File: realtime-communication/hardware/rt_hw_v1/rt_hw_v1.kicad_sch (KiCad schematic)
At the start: 64 parts, among them J1 USB2UART, J6 ConnBattery, Q1 SS8050, Q2 SS8050, SW1 RST, SW3 Boot, SW4 5V_EN, SW9 PS Joystick, U1 74HCT245_TSSOP, U2 CH340C, U3 ESP32-S3-WROOM-1, U4 BQ27441-G1, U5 BQ24075RGT_DPPM, U6 TPS63002_SEPIC_5V, U7 ADS1115IDGS, U9 TPS63001_SEPIC_3V3

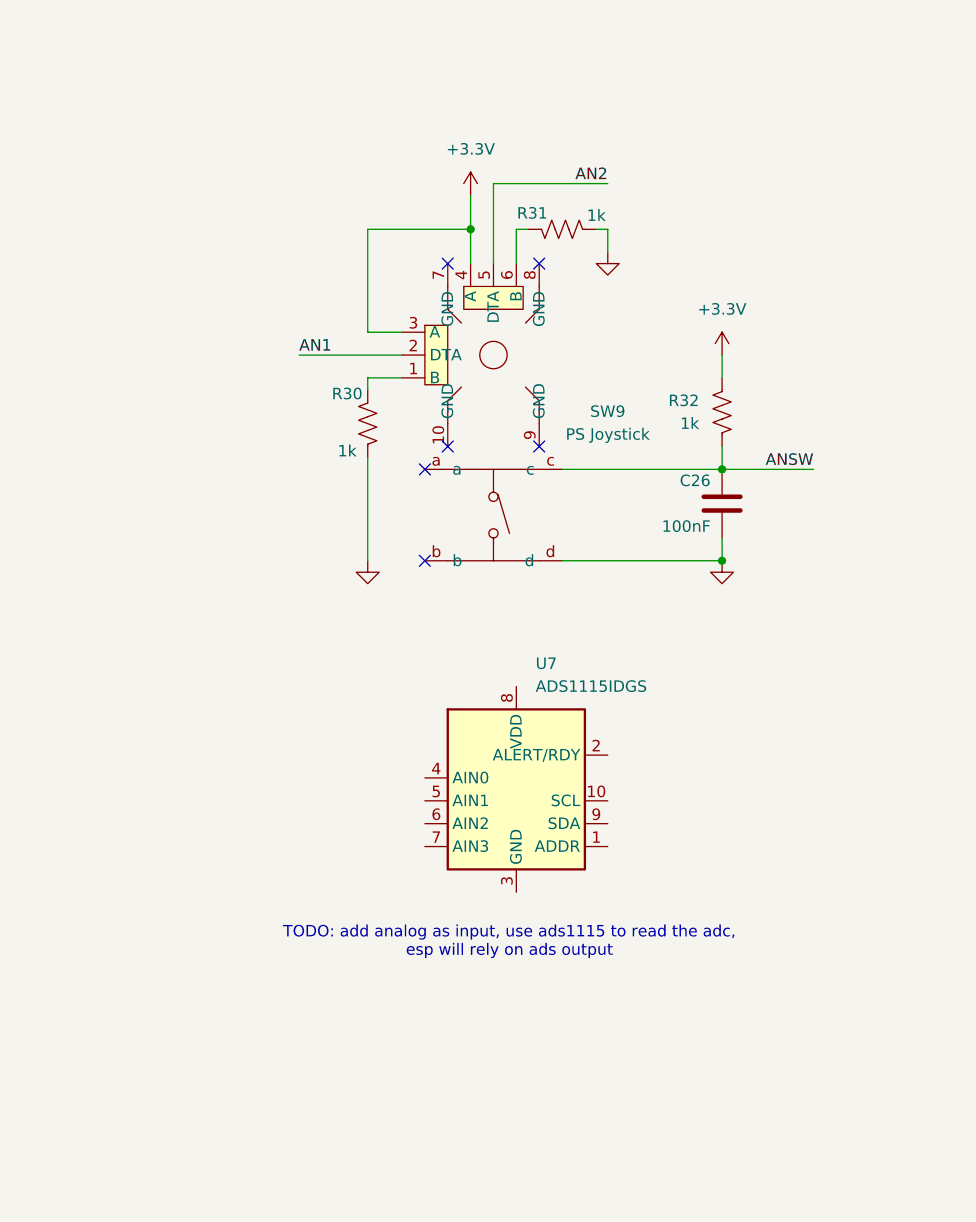
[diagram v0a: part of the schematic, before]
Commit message: add ads1115 from design block
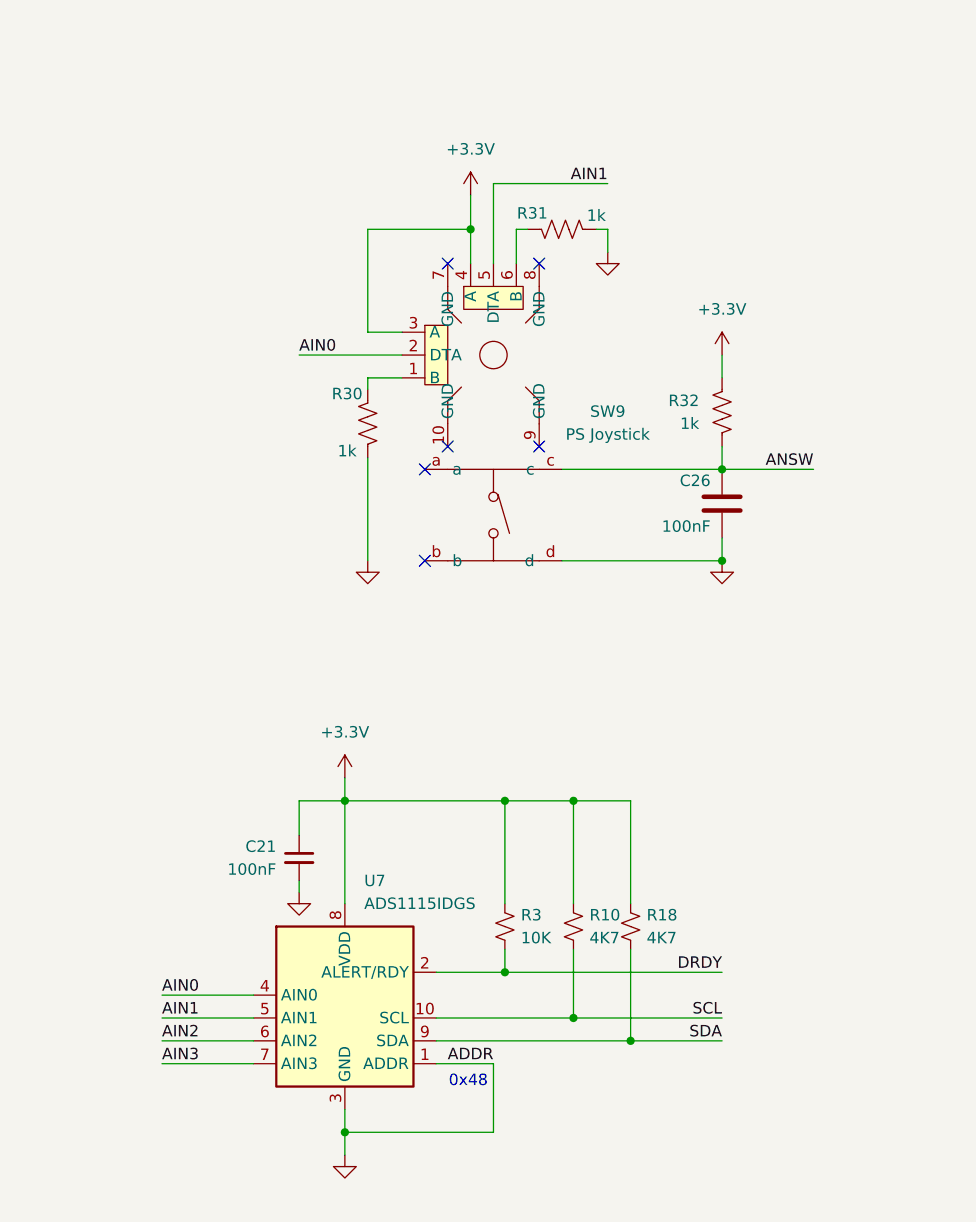
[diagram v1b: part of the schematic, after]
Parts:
- added C21: 100nF, Capacitor_SMD:C_0805_2012Metric, symbol Device:C_Small
- added R10, R18: 4K7, Resistor_SMD:R_0805_2012Metric, symbol Device:R_Small_US
- added R3: 10K, Resistor_SMD:R_0805_2012Metric, symbol Device:R_Small_US
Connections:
- net AN1 is gone; now on net AIN0: SW9.2 (DTA)
- net AN2 is gone; now on net AIN1: SW9.5 (DTA)
- net +3.3V: now also U7.8 (VDD), C21.1, R10.1, R18.1, R3.1
- net GND: now also U7.1 (ADDR), U7.3 (GND), C21.2
- net SCL: now reaches U7.10 (SCL)
- net SCL: now also R10.2
- net DRDY: now reaches U7.2 (ALERT/RDY)
- net DRDY: now also R3.2
- net AIN0: now reaches U7.4 (AIN0)
- net AIN1: now reaches U7.5 (AIN1)
- net AIN2: now reaches U7.6 (AIN2)
- net AIN3: now reaches U7.7 (AIN3)
- net SDA: now reaches U7.9 (SDA)
- net SDA: now also R18.2
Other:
- note added: "0x48"
- note removed: "TODO: add analog as input, use ads1115 to read the adc, esp will rely on ads output"

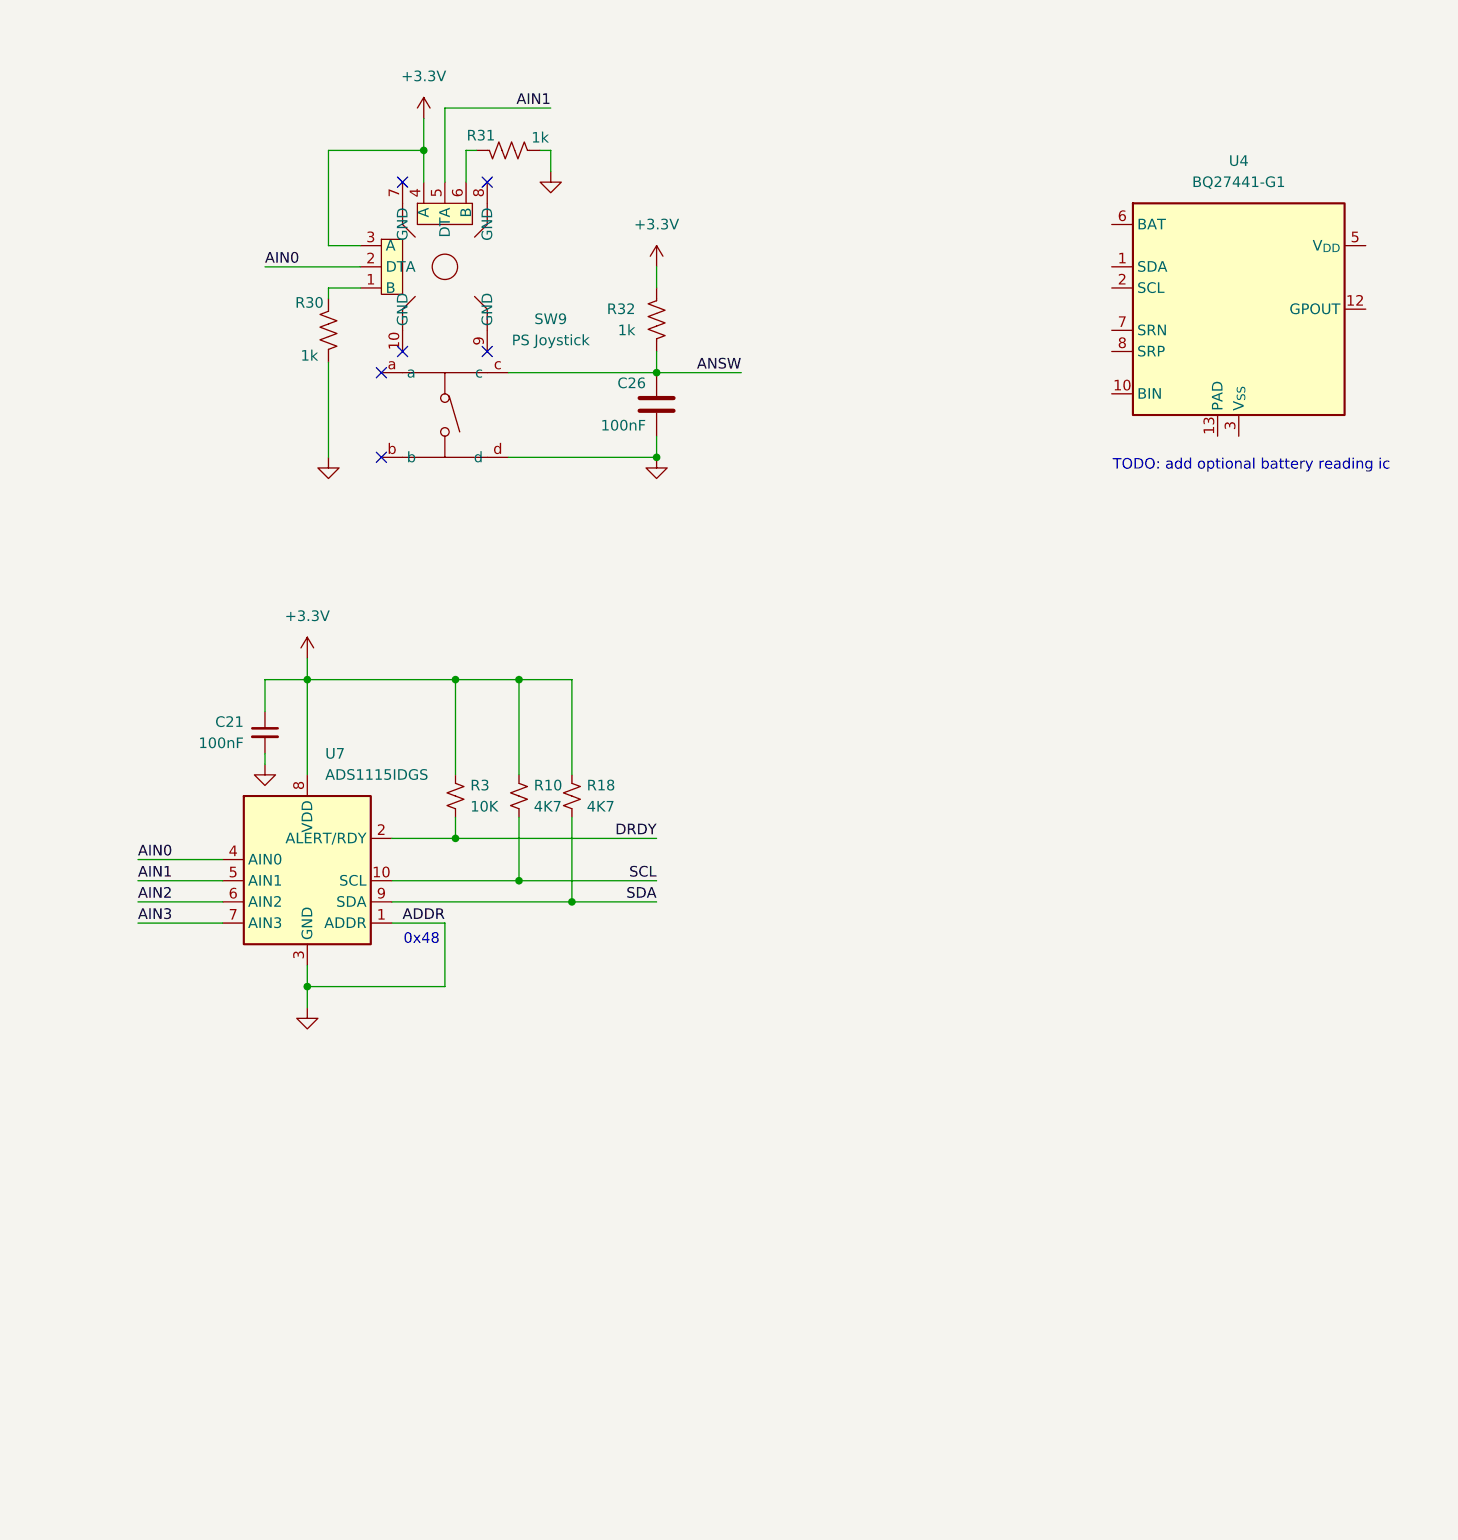
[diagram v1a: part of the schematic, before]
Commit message: add bq27441 single batt fuel gauge
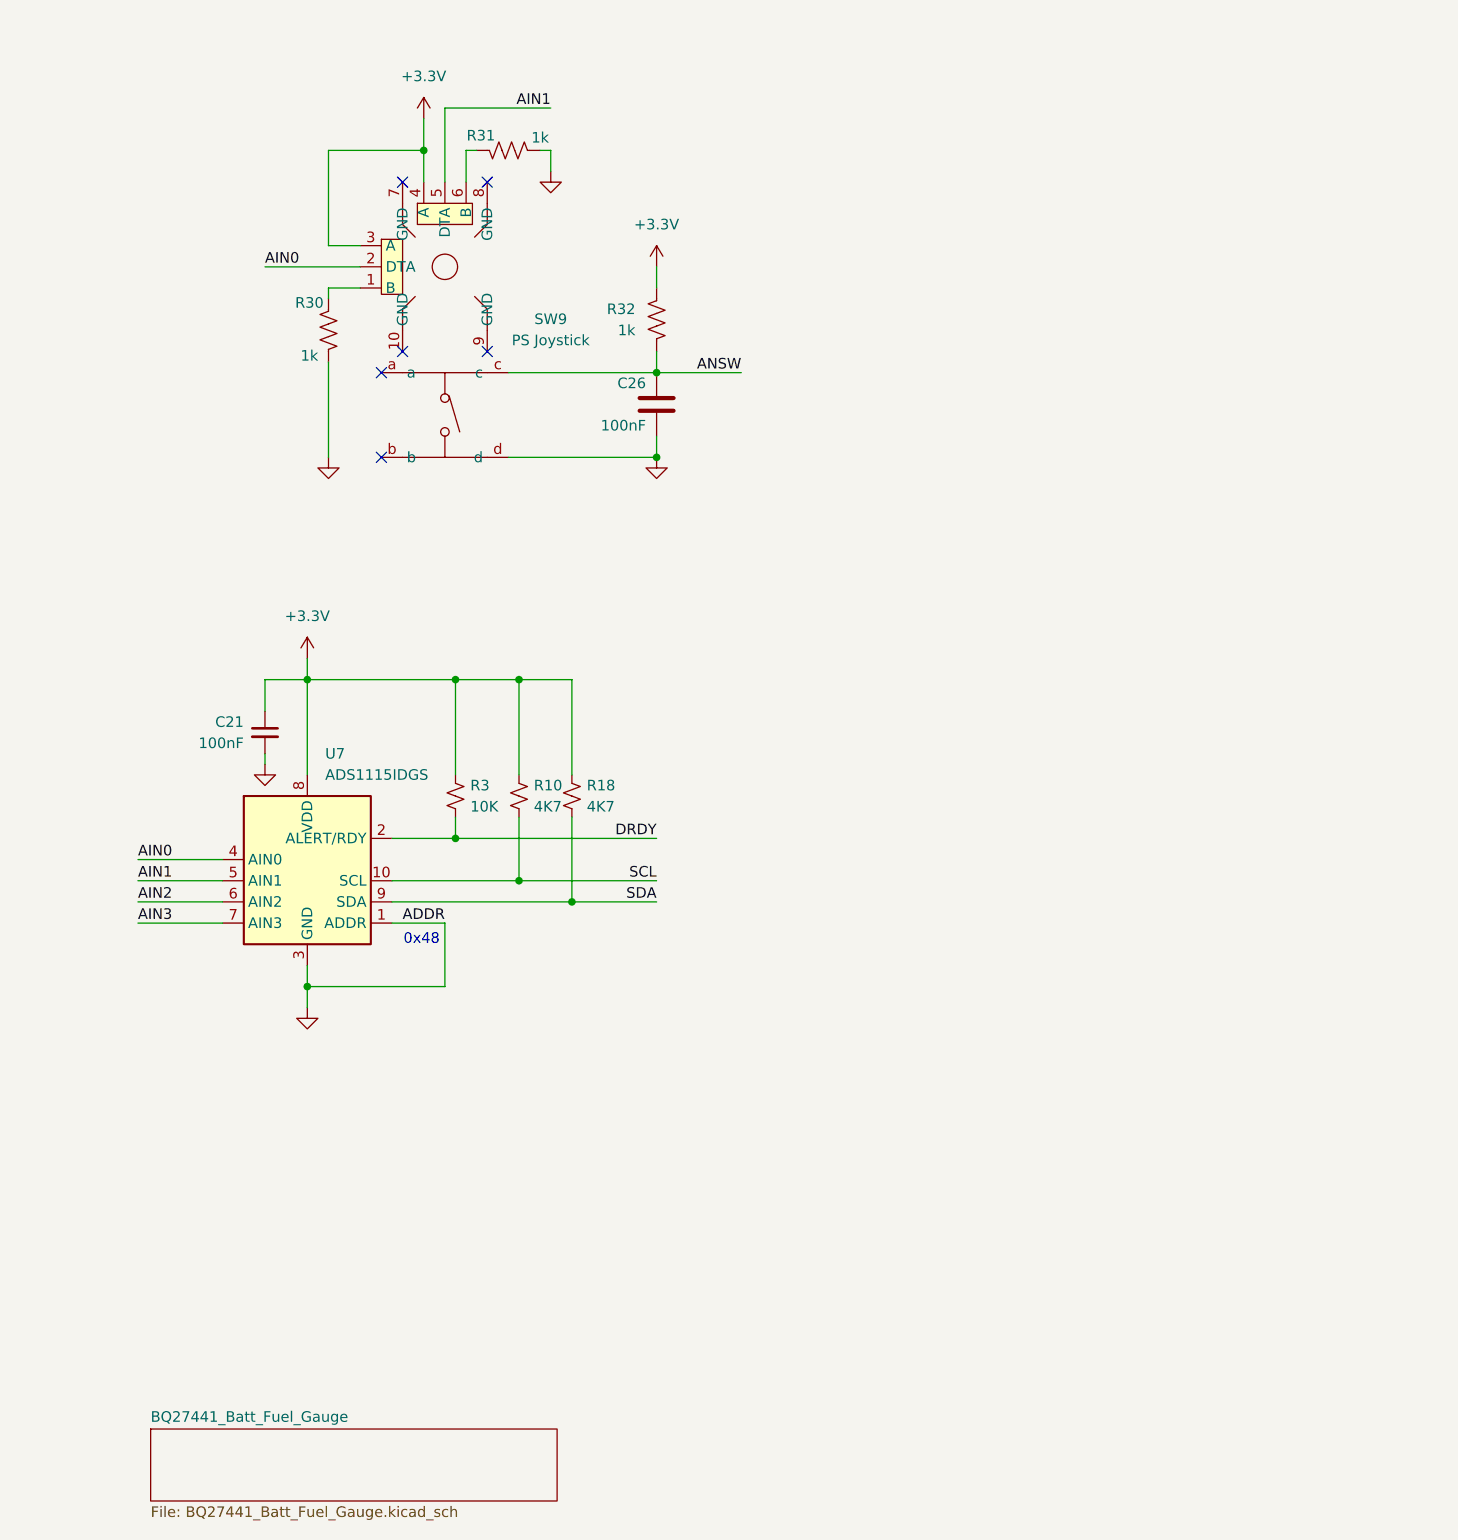
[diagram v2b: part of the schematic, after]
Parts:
- removed U4: BQ27441-G1, Package_SON:Texas_S-PDSO-N12, symbol Battery_Management:BQ27441-G1
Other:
- added sheet BQ27441_Batt_Fuel_Gauge (BQ27441_Batt_Fuel_Gauge.kicad_sch)
- note removed: "TODO: add optional battery reading ic"
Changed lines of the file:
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@@
 		)
 	)
-	(text "TODO: add optional battery reading ic "
-		(exclude_from_sim no)
-		(at 447.294 117.856 0)
-		(effects
-			(font
-				(size 1.27 1.27)
-			)
-		)
-	)
 	(text "Program the Input Current Limit (ILIM)\nRILIM = KILIM / II_MAX\nKILIM = 1550 AΩ from the electrical characteristics table.\nRISET = 1550 AΩ / 1.3 A = 1.192 kΩ -> 1.18 kΩ"
 		(exclude_from_sim no)
@@
 	)
 	(symbol
-		(lib_id "Battery_Management:BQ27441-G1")
-		(at 445.77 99.06 0)
-		(unit 1)
-		(body_style 1)
-		(exclude_from_sim no)
-		(in_bom yes)
-		(on_board yes)
-		(in_pos_files yes)
-		(dnp no)
-		(fields_autoplaced yes)
-		(property "Reference" "U4"
-			(at 445.77 81.28 0)
-			(show_name no)
-			(do_not_autoplace no)
-			(effects
-				(font
-					(size 1.27 1.27)
-				)
-			)
-		)
-		(property "Value" "BQ27441-G1"
-			(at 445.77 83.82 0)
-			(show_name no)
-			(do_not_autoplace no)
-			(effects
-				(font
-					(size 1.27 1.27)
-				)
-			)
-		)
-		(property "Footprint" "Package_SON:Texas_S-PDSO-N12"
-			(at 452.12 113.03 0)
-			(hide yes)
-			(show_name no)
-			(do_not_autoplace no)
-			(effects
-				(font
-					(size 1.27 1.27)
-				)
-				(justify left)
-			)
-		)
-		(property "Datasheet" "http://www.ti.com/lit/ds/symlink/bq27441-g1.pdf"
-			(at 450.85 93.98 0)
-			(hide yes)
-			(show_name no)
-			(do_not_autoplace no)
-			(effects
-				(font
-					(size 1.27 1.27)
-				)
-			)
-		)
-		(property "Description" "System Side Li Ion/Polymer Fuel Gauge, PDSON-12"
-			(at 445.77 99.06 0)
-			(hide yes)
-			(show_name no)
-			(do_not_autoplace no)
-			(effects
-				(font
-					(size 1.27 1.27)
-				)
-			)
-		)
-		(pin "9"
-		)
-		(pin "13"
-		)
-		(pin "11"
-		)
-		(pin "10"
-		)
-		(pin "12"
-		)
-		(pin "1"
-		)
-		(pin "2"
-		)
-		(pin "3"
-		)
-		(pin "4"
-		)
-		(pin "5"
-		)
-		(pin "6"
-		)
-		(pin "7"
-		)
-		(pin "8"
-		)
-		(instances
-			(project "rt_hw_v1"
-				(path "/febfcd6e-7fe3-48d0-b229-7957d3116d0e"
-					(reference "U4")
-					(unit 1)
-				)
-			)
-		)
-	)
-	(symbol
 		(lib_id "LED:WS2812B-2020")
 		(at 85.09 50.8 0)
@@
 		)
 	)
+	(sheet
+		(at 315.214 233.426)
+		(size 48.768 8.636)
+		(exclude_from_sim no)
+		(in_bom yes)
+		(on_board yes)
+		(dnp no)
+		(fields_autoplaced yes)
+		(stroke
+			(width 0.1524)
+			(type solid)
+		)
+		(fill
+			(color 0 0 0 0)
+		)
+		(property "Sheetname" "BQ27441_Batt_Fuel_Gauge"
+			(at 315.214 232.7144 0)
+			(show_name no)
+			(do_not_autoplace no)
+			(effects
+				(font
+					(size 1.27 1.27)
+				)
+				(justify left bottom)
+			)
+		)
+		(property "Sheetfile" "BQ27441_Batt_Fuel_Gauge.kicad_sch"
+			(at 315.214 242.6466 0)
+			(show_name no)
+			(do_not_autoplace no)
+			(effects
+				(font
+					(size 1.27 1.27)
+				)
+				(justify left top)
+			)
+		)
+		(instances
+			(project "rt_hw_v1"
+				(path "/febfcd6e-7fe3-48d0-b229-7957d3116d0e"
+					(page "2")
+				)
+			)
+		)
+	)
